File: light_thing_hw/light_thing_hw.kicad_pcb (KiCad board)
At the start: 2 copper layers, 22 parts, among them J1 SWD_PINS, J2 LiPo Battery, U1 BQ24075, U2 LSM6DS3, U3 BC832-V1, U5A1 STM32L452RETx

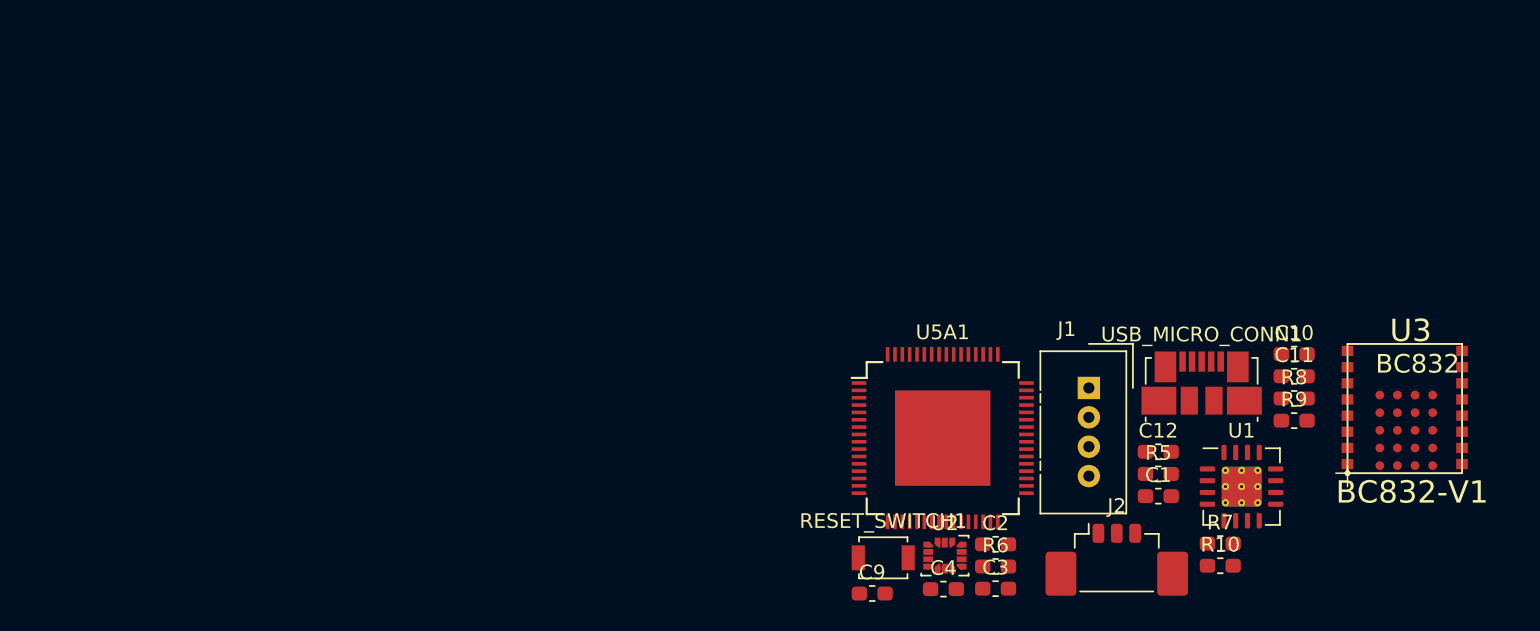
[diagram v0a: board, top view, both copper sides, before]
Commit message: updates on hw design. it seems like we can make it on a 3x3cm pcb. layout needs work
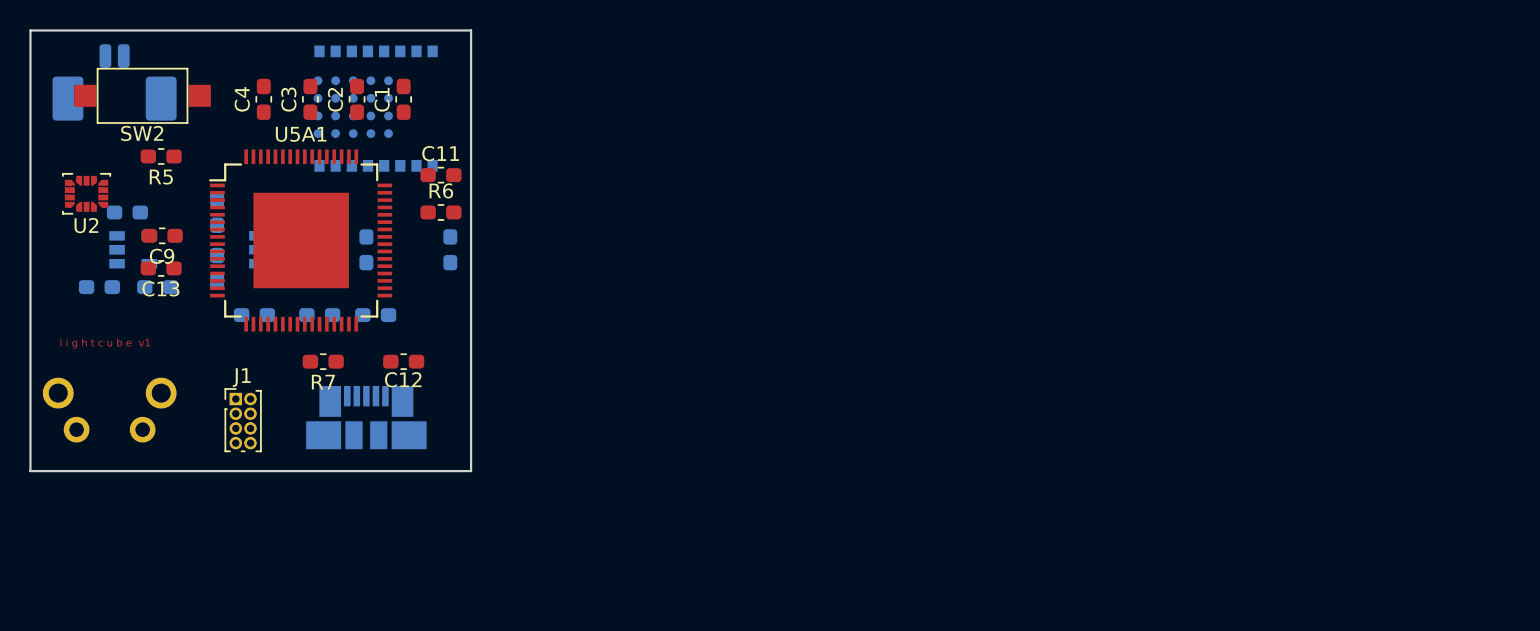
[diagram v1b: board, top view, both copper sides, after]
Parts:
- removed R10, R9: 1.5k, Resistor_SMD:R_0603_1608Metric_Pad1.05x0.95mm_HandSolder
- removed R8: 1.13k, Resistor_SMD:R_0603_1608Metric_Pad1.05x0.95mm_HandSolder
- removed RESET_SWITCH1: SW_Push_Dual_x2, Button_Switch_SMD:SW_SPST_B3U-1000P
- added C13: 100nF, Capacitor_SMD:C_0603_1608Metric_Pad1.05x0.95mm_HandSolder, F.Cu at (88.9, 76.2)
- added C5: 4.7uF, Capacitor_SMD:C_0603_1608Metric_Pad1.05x0.95mm_HandSolder, B.Cu at (84.7, 77.5)
- added C6: 4.7uF, Capacitor_SMD:C_0603_1608Metric_Pad1.05x0.95mm_HandSolder, B.Cu at (86.6, 72.4)
- added C7: C_Small, Capacitor_SMD:C_0603_1608Metric_Pad1.05x0.95mm_HandSolder, B.Cu at (103.5, 79.4)
- added C8: 10uF, Capacitor_SMD:C_0603_1608Metric_Pad1.05x0.95mm_HandSolder, B.Cu at (92.7, 72.4)
- added D1: 2.5A, Diode_SMD:D_0603_1608Metric_Pad1.05x0.95mm_HandSolder, B.Cu at (99.7, 79.4)
- added L1: 10uH, 2.5A, Inductor_SMD:L_0603_1608Metric_Pad1.05x0.95mm_HandSolder, B.Cu at (95.2, 79.4)
- added R1: 2k, Resistor_SMD:R_0603_1608Metric_Pad1.05x0.95mm_HandSolder, B.Cu at (88.7, 77.5)
- added R2: 1M, Resistor_SMD:R_0603_1608Metric_Pad1.05x0.95mm_HandSolder, B.Cu at (99.7, 74.9)
- added R3: 30.1k, Resistor_SMD:R_0603_1608Metric_Pad1.05x0.95mm_HandSolder, B.Cu at (108.6, 74.9)
- added R4: 10k, Resistor_SMD:R_0603_1608Metric_Pad1.05x0.95mm_HandSolder, B.Cu at (102.9, 74.9)
- added SW1: ST_USER_BUTTON1, Button_Switch_THT:SW_Tactile_SPST_Angled_PTS645Vx39-2LFS, B.Cu at (83.1, 87.2)
- added SW2: ST_RESET_BUTTON, Button_Switch_SMD:SW_SPST_CK_RS282G05A3, F.Cu at (87.6, 64.5)
- added U4: LMR62421XMF, Package_TO_SOT_SMD:SOT-23-5, B.Cu at (96.5, 74.9)
- C10: value 4.7uF -> 10uF; moved to B.Cu
- C11: value 1uF -> 100nF
- C12: value 4.7uF -> 1nF
- J1: value SWD_PINS -> CONNECTORS; footprint Connector:NS-Tech_Grove_1x04_P2mm_Vertical -> Connector_PinHeader_1.00mm:PinHeader_2x04_P1.00mm_Vertical
- J2: value LiPo Battery -> Li-Ion Battery; footprint Connector_Molex:Molex_PicoBlade_53398-0371_1x03-1MP_P1.25mm_Vertical -> Connector_Molex:Molex_PicoBlade_53261-0271_1x02-1MP_P1.25mm_Horizontal; moved to B.Cu
- R6: value 100k -> R
- R7: value 1.18k -> R
- U1: value BQ24075 -> BC832-V1; footprint Package_DFN_QFN:QFN-16-1EP_5x5mm_P0.8mm_EP2.7x2.7mm_ThermalVias -> Fanstel_modules:BC832-BC832; moved to B.Cu
- U3: value BC832-V1 -> MCP73832-2-OT; footprint Fanstel_modules:BC832-BC832 -> Package_TO_SOT_SMD:SOT-23-5; moved to B.Cu
- USB_MICRO_CONN1: moved to B.Cu
- moved U3 84.1 mm to (87.0, 74.9)
- moved J2 75.1 mm to (85.7, 64.1), turned to 180 degrees
- moved C10 73.6 mm to (92.7, 76.2), turned to 270 degrees
- moved R5 71.2 mm to (88.9, 68.6), turned to 180 degrees
- moved U1 67.1 mm to (99.1, 69.2), turned to 90 degrees
- moved U2 63.4 mm to (83.8, 71.1), turned to 180 degrees
- moved R7 62.3 mm to (99.9, 82.5), turned to 180 degrees
- moved C11 59.7 mm to (108.0, 69.8)
- moved J1 58.1 mm to (94.0, 85.1)
- moved C1 58.1 mm to (105.4, 64.7), turned to 90 degrees
- moved C3 57.3 mm to (99.1, 64.7), turned to 90 degrees
- moved C4 57.0 mm to (95.9, 64.7), turned to 90 degrees
- moved USB_MICRO_CONN1 56.9 mm to (102.9, 86.4), turned to 180 degrees
- moved C9 54.1 mm to (89.0, 74.0), turned to 180 degrees
- moved C2 53.0 mm to (102.2, 64.7), turned to 90 degrees
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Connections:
- net Net-(U5A1-Pad14) renamed ADDR_LED_BACKUP_PWM
- C1 pad 2: GND -> +5V
- C10 pad 1: GND -> +5V
- C10 pad 2: +BATT -> +5V
- C11 pad 1: VBUS -> +3V3
- C11 pad 2: GND -> +5V
- C12 pad 1: GND -> +5V
- C12 pad 2: CHG_OUT -> Net-(C12-Pad2)
- C2 pad 2: GND -> +5V
- C3 pad 2: GND -> +5V
- C4 pad 2: GND -> +5V
- C9 pad 2: GND -> +5V
- J1 pad 1: Net-(J1-Pad1) -> SWCLK
- J1 pad 2: Net-(J1-Pad2) -> SWDIO
- J1 pad 3: Net-(J1-Pad3) -> RESET
- J1 pad 4: Net-(J1-Pad4) -> USART_2_RX
- J2 pad 1: GND -> +5V
- J2 pad 2: CHG_TS -> +BATT
- R5 pad 2: GND -> +5V
- R6 pad 1: GND -> +3V3
- R6 pad 2: CHARGER_CE -> +5V
- R7 pad 1: Net-(R7-Pad1) -> +5V
- R7 pad 2: GND -> Net-(C13-Pad2)
- U2 pad 1: Net-(U2-Pad1) -> +5V
- U2 pad 2: Net-(U2-Pad2) -> +5V
- U2 pad 3: Net-(U2-Pad3) -> +5V
- U2 pad 4: Net-(U2-Pad4) -> ACCEL_EXTI_1
- U2 pad 5: Net-(U2-Pad5) -> +3V3
- U2 pad 6: GND -> +5V
- U2 pad 7: GND -> +5V
- U2 pad 8: Net-(U2-Pad8) -> +3V3
- U2 pad 9: Net-(U2-Pad9) -> ACCEL_EXTI_2
- U5A1 pad 12: GND -> +5V
- U5A1 pad 18: GND -> +5V
- U5A1 pad 2: Net-(U5A1-Pad2) -> BUTTON1
- U5A1 pad 31: GND -> +5V
- U5A1 pad 34: Net-(U5A1-Pad34) -> I2C2_SCL
- U5A1 pad 35: Net-(U5A1-Pad35) -> I2C2_SDA
- U5A1 pad 42: Net-(U5A1-Pad42) -> I2C1_SCL
- U5A1 pad 43: Net-(U5A1-Pad43) -> I2C1_SDA
- U5A1 pad 44: Net-(U5A1-Pad44) -> D-
- U5A1 pad 45: Net-(U5A1-Pad45) -> D+
- U5A1 pad 47: GND -> +5V
- U5A1 pad 51: Net-(U5A1-Pad51) -> BT_RX
- U5A1 pad 52: Net-(U5A1-Pad52) -> BT_TX
- U5A1 pad 58: Net-(U5A1-Pad58) -> ACCEL_EXTI_1
- U5A1 pad 59: Net-(U5A1-Pad59) -> ACCEL_EXTI_2
- U5A1 pad 63: GND -> +5V
- USB_MICRO_CONN1 pad 5: GND -> +5V
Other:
- board outline added: 30 x 30 mm
- board text added: "l i g h t c u b e v1"

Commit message: hw updates
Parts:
- added 1k1: R, Resistor_SMD:R_0603_1608Metric_Pad1.05x0.95mm_HandSolder, F.Cu at (214.0, 57.0)
- added C14: 10uF, Capacitor_SMD:C_0603_1608Metric_Pad1.05x0.95mm_HandSolder, F.Cu at (233.1, 80.0)
- added C16: 0.1uF, Capacitor_SMD:C_0603_1608Metric_Pad1.05x0.95mm_HandSolder, F.Cu at (230.1, 45.0)
- added C17: 0.1uF, Capacitor_SMD:C_0603_1608Metric_Pad1.05x0.95mm_HandSolder, F.Cu at (214.1, 53.0)
- added D2: GREEN LED, LED_SMD:LED_1806_4516Metric_Pad1.57x1.80mm_HandSolder, F.Cu at (164.0, 50.0)
- added D3: RED LED, LED_SMD:LED_1806_4516Metric_Pad1.57x1.80mm_HandSolder, F.Cu at (159.9, 50.0)
- added J3: ADDR_LED_PANEL_1_CONNECTORS, Connector_PinHeader_1.00mm:PinHeader_2x02_P1.00mm_Vertical, F.Cu at (172.0, 71.0)
- added J4: ADDR_LED_PANEL_2_CONNECTORS, Connector_PinHeader_1.00mm:PinHeader_2x02_P1.00mm_Vertical, F.Cu at (168.0, 71.0)
- added Q1: MMBF170, Package_TO_SOT_SMD:SOT-23, F.Cu at (185.0, 64.0)
- added R10: 4.7k, Resistor_SMD:R_0603_1608Metric_Pad1.05x0.95mm_HandSolder, F.Cu at (236.1, 44.0)
- added R11: 4.7k, Resistor_SMD:R_0603_1608Metric_Pad1.05x0.95mm_HandSolder, F.Cu at (225.1, 53.0)
- added R12: 4.7k, Resistor_SMD:R_0603_1608Metric_Pad1.05x0.95mm_HandSolder, F.Cu at (230.1, 53.0)
- added R13: 4.7k, Resistor_SMD:R_0603_1608Metric_Pad1.05x0.95mm_HandSolder, F.Cu at (235.9, 48.0)
- added R14: 1k, Resistor_SMD:R_0603_1608Metric_Pad1.05x0.95mm_HandSolder, F.Cu at (235.1, 57.0)
- added R15: 3.5k, Resistor_SMD:R_0603_1608Metric_Pad1.05x0.95mm_HandSolder, F.Cu at (238.1, 81.0)
- added R16: 3.5k, Resistor_SMD:R_0603_1608Metric_Pad1.05x0.95mm_HandSolder, F.Cu at (222.0, 84.0)
- added R8: 510, Resistor_SMD:R_0603_1608Metric_Pad1.05x0.95mm_HandSolder, F.Cu at (240.9, 48.0)
- added R9: 510, Resistor_SMD:R_0603_1608Metric_Pad1.05x0.95mm_HandSolder, F.Cu at (230.0, 57.0)
- added U5: LP38511MRX-ADJ_NOPB, footprints:LP38511MRX-ADJ_NOPB, B.Cu at (185.0, 76.0)
- C1, C2, C3, C4: value 100 nF -> 0.1uF
- C10, C7, C8, L1, R2, R3, R4: moved to F.Cu
- C5, C6: value 4.7uF -> 1uF; moved to F.Cu
- D1: value 2.5A -> 2.5A, 20V; footprint Diode_SMD:D_0603_1608Metric_Pad1.05x0.95mm_HandSolder -> Diode_SMD:D_SOD-323_HandSoldering; moved to F.Cu
- J1: footprint Connector_PinHeader_1.00mm:PinHeader_2x04_P1.00mm_Vertical -> Connector_PinHeader_1.00mm:PinHeader_2x05_P1.00mm_Vertical
- R1: value 2k -> 800; moved to F.Cu
- U1: footprint Fanstel_modules:BC832-BC832 -> Fanstel_modules:BC832-BC832_3d1
- U3: value MCP73832-2-OT -> MCP73833T-FCI_MF; footprint Package_TO_SOT_SMD:SOT-23-5 -> footprints:MCP73833T-FCI&slash_MF
- moved R5 159.1 mm to (246.1, 44.0), turned to 0 degrees
- moved C10 156.3 mm to (249.0, 78.0), turned to 0 degrees
- moved R1 155.2 mm to (243.9, 78.0), turned to 0 degrees
- moved C13 153.0 mm to (240.1, 53.0), turned to 0 degrees
- moved C8 151.5 mm to (243.9, 83.0), turned to 0 degrees
- moved C3 148.0 mm to (246.1, 48.0), turned to 0 degrees
- moved R7 146.2 mm to (241.0, 44.0), turned to 0 degrees
- moved C2 144.2 mm to (246.0, 53.0), turned to 0 degrees
- moved C6 136.8 mm to (222.4, 89.0), turned to 0 degrees
- moved C5 136.3 mm to (221.0, 79.0)
- moved C1 134.9 mm to (240.1, 57.0), turned to 0 degrees
- moved R2 133.7 mm to (233.0, 85.0), turned to 0 degrees
- moved C9 132.7 mm to (220.0, 53.0), turned to 0 degrees
- moved R3 130.1 mm to (238.1, 87.0), turned to 0 degrees
- moved C4 129.3 mm to (225.0, 57.0), turned to 0 degrees
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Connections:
- net BOOT0 renamed Net-(R5-Pad1)
- net USB_ID renamed Net-(USB_MICRO_CONN1-Pad4)
- C5 pad 1: +BATT -> VBUS
- C6 pad 1: +3V3 -> +BATT
- C8 pad 2: +3V3 -> +BATT
- D1 pad 1: Net-(D1-Pad1) -> +5V
- D1 pad 2: +5V -> Net-(D1-Pad2)
- J1 pad 1: SWCLK -> USART_2_RX
- J1 pad 2: SWDIO -> USART_2_TX
- J1 pad 3: RESET -> BT_RX
- J1 pad 4: USART_2_RX -> BT_TX
- J1 pad 5: USART_2_TX -> SWCLK
- J1 pad 6: BT_SWCLK -> SWDIO
- J1 pad 7: BT_SWDIO -> RESET
- J1 pad 8: BT_RST -> BT_SWCLK
- L1 pad 1: +3V3 -> +BATT
- L1 pad 2: Net-(D1-Pad1) -> Net-(D1-Pad2)
- R1 pad 1: Net-(R1-Pad1) -> +5V
- R1 pad 2: +5V -> Net-(R1-Pad2)
- R2 pad 2: +3V3 -> +BATT
- U1 pad P$11: Net-(U1-PadP$11) -> BT_GPIO_2
- U1 pad P$12: Net-(U1-PadP$12) -> BT_GPIO_1
- U1 pad P$13: Net-(U1-PadP$13) -> BT_GPIO_0
- U1 pad P$16: Net-(U1-PadP$16) -> +3V3
- U1 pad P$6: Net-(U1-PadP$6) -> BT_RED_LED
- U1 pad P$9: Net-(U1-PadP$9) -> BT_GPIO_3
- U3 pad 1: Net-(U3-Pad1) -> VBUS
- U3 pad 2: +5V -> VBUS
- U3 pad 3: +BATT -> Net-(U3-Pad3)
- U3 pad 4: +3V3 -> Net-(U3-Pad4)
- U3 pad 5: Net-(R1-Pad1) -> +5V
- U4 pad 1: Net-(D1-Pad1) -> Net-(D1-Pad2)
- U4 pad 5: +3V3 -> +BATT
- U5A1 pad 1: Net-(U5A1-Pad1) -> +3V3
- U5A1 pad 10: Net-(U5A1-Pad10) -> BT_GPIO_0
- U5A1 pad 11: Net-(U5A1-Pad11) -> BT_GPIO_1
- U5A1 pad 21: Net-(U5A1-Pad21) -> GREEN_LED
- U5A1 pad 22: Net-(U5A1-Pad22) -> BATT_ADC
- U5A1 pad 24: Net-(U5A1-Pad24) -> BT_GPIO_2
- U5A1 pad 25: Net-(U5A1-Pad25) -> BT_GPIO_3
- U5A1 pad 37: Net-(U5A1-Pad37) -> BATT_ADC_ENABLE
- U5A1 pad 48: Net-(U5A1-Pad48) -> +3V3
- USB_MICRO_CONN1 pad 2: D+ -> D-
- USB_MICRO_CONN1 pad 3: D- -> D+
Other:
- board outline removed
- rule pad_to_mask_clearance: 0.051 -> 0
- board text removed: "l i g h t c u b e v1"
